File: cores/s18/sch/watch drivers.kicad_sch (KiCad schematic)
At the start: 10 parts, among them Q10 74LS367, T10 74LS163, T11 PAL16L8

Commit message: wip cer
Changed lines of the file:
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@@
     (stroke (width 0) (type default) (color 0 0 0 0))
   )
-  (wire (pts (xy 215.9 85.09) (xy 204.47 85.09))
+  (wire (pts (xy 207.01 85.09) (xy 204.47 85.09))
     (stroke (width 0) (type default) (color 0 0 0 0))
   )
@@
     (effects (font (size 1.27 1.27)) (justify left bottom))
   )
-  (label "~{RST_CLK}" (at 215.9 85.09 180)
-    (effects (font (size 1.27 1.27)) (justify right bottom))
-  )
   (label "VSS" (at 182.88 64.77 0)
     (effects (font (size 1.27 1.27)) (justify left bottom))
@@
     (effects (font (size 1.27 1.27)) (justify left))
   )
+  (hierarchical_label "~{RST_CLK}" (shape tri_state) (at 207.01 85.09 0)
+    (effects (font (size 1.27 1.27)) (justify left))
+  )

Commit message: finished extraction of s18
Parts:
- removed 4.7kΩ: R31, symbol Device:R_US
- added R31: 4.7KΩ, symbol Device:R_US
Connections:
- net VCC: now also R31.1
- net ~{CSYNC}: now also R31.2
- net COUN_~{MR} renamed SPRPAL8
- net COUN_~{MR}B renamed MAPP_WR_H
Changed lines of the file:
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@@
     (rev "José Tejada G.")
     (company "JOTEGO")
-    (comment 1 "Esperanza Triana")
+    (comment 1 "patreon.com/jotego")
+    (comment 2 "Esperanza Triana")
   )
   (junction (at 60.96 138.43) (diameter 0) (color 0 0 0 0)
   )
+  (junction (at 146.05 110.49) (diameter 0) (color 0 0 0 0)
+  )
   (junction (at 60.96 87.63) (diameter 0) (color 0 0 0 0)
   )
@@
   )
   (junction (at 60.96 125.73) (diameter 0) (color 0 0 0 0)
-  )
-  (junction (at 146.05 110.49) (diameter 0) (color 0 0 0 0)
   )
   (junction (at 60.96 88.9) (diameter 0) (color 0 0 0 0)
@@
   (no_connect (at 146.05 125.73))
   (no_connect (at 182.88 53.34))
+  (bus_entry (at 46.99 106.68) (size 2.54 2.54)
+    (stroke (width 0) (type default) (color 0 0 0 0))
+  )
   (wire (pts (xy 115.57 130.81) (xy 115.57 152.4))
     (stroke (width 0) (type default) (color 0 0 0 0))
@@
     (stroke (width 0) (type default) (color 0 0 0 0))
   )
-  (wire (pts (xy 185.42 80.01) (xy 172.72 80.01))
+  (wire (pts (xy 185.42 80.01) (xy 180.34 80.01))
     (stroke (width 0) (type default) (color 0 0 0 0))
   )
@@
     (stroke (width 0) (type default) (color 0 0 0 0))
   )
-  (wire (pts (xy 50.8 147.32) (xy 60.96 147.32))
+  (wire (pts (xy 41.91 147.32) (xy 60.96 147.32))
     (stroke (width 0) (type default) (color 0 0 0 0))
   )
@@
     (stroke (width 0) (type default) (color 0 0 0 0))
   )
+  (bus (pts (xy 41.91 106.68) (xy 46.99 106.68))
+    (stroke (width 0) (type default) (color 0 0 0 0))
+  )
   (wire (pts (xy 100.33 88.9) (xy 100.33 93.98))
     (stroke (width 0) (type default) (color 0 0 0 0))
@@
     (stroke (width 0) (type default) (color 0 0 0 0))
   )
-  (image (at 275.59 175.26) (scale 0.25)
+  (image (at 276.86 173.99) (scale 0.198066)
     (data
       iVBORw0KGgoAAAANSUhEUgAAAxoAAAMaCAIAAACOIqcFAAAAA3NCSVQICAjb4U/gAAAACXBIWXMA
@@
     (effects (font (size 1.27 1.27)) (justify right bottom))
   )
-  (label "COUN_~{MR}B" (at 110.49 128.27 0)
-    (effects (font (size 1.27 1.27)) (justify left bottom))
-  )
   (label "VSS" (at 162.56 52.07 180)
     (effects (font (size 1.27 1.27)) (justify right bottom))
   )
-  (label "COUN_~{MR}" (at 110.49 120.65 0)
-    (effects (font (size 1.27 1.27)) (justify left bottom))
-  )
-  (label "COUN_~{MR}B" (at 50.8 147.32 0)
+  (label "SPRPAL8" (at 110.49 120.65 0)
     (effects (font (size 1.27 1.27)) (justify left bottom))
   )
@@
     (effects (font (size 1.27 1.27)) (justify left bottom))
   )
-  (label "COUN_~{MR}" (at 110.49 83.82 0)
+  (label "SPRPAL8" (at 110.49 83.82 0)
+    (effects (font (size 1.27 1.27)) (justify left bottom))
+  )
+  (label "MAPP_WR_H" (at 110.49 128.27 0)
     (effects (font (size 1.27 1.27)) (justify left bottom))
   )
@@
     (effects (font (size 1.27 1.27)) (justify right bottom))
   )
+  (label "SPRPAL8" (at 49.53 109.22 0)
+    (effects (font (size 1.27 1.27)) (justify left bottom))
+  )
   (label "VCC" (at 53.34 100.33 0)
     (effects (font (size 1.27 1.27)) (justify left bottom))
@@
     (effects (font (size 1.27 1.27)) (justify left bottom))
   )
-  (label "~{RESET}" (at 172.72 80.01 0)
-    (effects (font (size 1.27 1.27)) (justify left bottom))
-  )
-  (label "COUN_~{MR}B" (at 110.49 128.27 0)
-    (effects (font (size 1.27 1.27)) (justify left bottom))
-  )
   (label "VSS" (at 180.34 100.33 0)
     (effects (font (size 1.27 1.27)) (justify left bottom))
@@
   )
   (label "VSS" (at 53.34 125.73 0)
-    (effects (font (size 1.27 1.27)) (justify left bottom))
-  )
-  (label "COUN_~{MR}" (at 49.53 109.22 0)
     (effects (font (size 1.27 1.27)) (justify left bottom))
   )
@@
     (effects (font (size 1.27 1.27)) (justify left))
   )
+  (hierarchical_label "SPRPAL[10..1]" (shape input) (at 41.91 106.68 180)
+    (effects (font (size 1.27 1.27)) (justify right))
+  )
   (hierarchical_label "~{VSYNC}" (shape input) (at 180.34 82.55 180)
     (effects (font (size 1.27 1.27)) (justify right))
@@
     (effects (font (size 1.27 1.27)) (justify right))
   )
+  (hierarchical_label "~{RESET}" (shape input) (at 180.34 80.01 180)
+    (effects (font (size 1.27 1.27)) (justify right))
+  )
   (hierarchical_label "SYNC" (shape tri_state) (at 213.36 43.18 0)
     (effects (font (size 1.27 1.27)) (justify left))
@@
   )
   (hierarchical_label "PRE_SYNC" (shape input) (at 176.53 43.18 180)
+    (effects (font (size 1.27 1.27)) (justify right))
+  )
+  (hierarchical_label "MAPP_WR_H" (shape input) (at 41.91 147.32 180)
     (effects (font (size 1.27 1.27)) (justify right))
   )
@@
     (pin "7")
   )
+  (symbol (lib_id "Device:R_US") (at 146.05 114.3 0) (unit 1)
+    (in_bom yes) (on_board yes)
+    (property "Reference" "R31" (id 0) (at 149.86 113.03 0))
+    (property "Value" "4.7KΩ" (id 1) (at 149.86 115.57 0))
+    (property "Footprint" "" (id 2) (at 147.066 114.554 90)
+      (effects (font (size 1.27 1.27)) hide)
+    )
+    (property "Datasheet" "~" (id 3) (at 146.05 114.3 0)
+      (effects (font (size 1.27 1.27)) hide)
+    )
+    (pin "1")
+    (pin "2")
+  )
   (symbol (lib_id "jt74:74LS163") (at 73.66 96.52 0) (unit 1)
     (in_bom yes) (on_board yes)
@@
     (pin "9")
   )
-  (symbol (lib_id "Device:R_US") (at 146.05 114.3 0) (unit 1)
-    (in_bom yes) (on_board yes)
-    (property "Reference" "4.7kΩ" (id 0) (at 149.86 116.84 0))
-    (property "Value" "R31" (id 1) (at 148.59 114.3 0))
-    (property "Footprint" "" (id 2) (at 147.066 114.554 90)
-      (effects (font (size 1.27 1.27)) hide)
-    )
-    (property "Datasheet" "~" (id 3) (at 146.05 114.3 0)
-      (effects (font (size 1.27 1.27)) hide)
-    )
-    (pin "1")
-    (pin "2")
-  )
   (symbol (lib_id "Device:C_Small") (at 162.56 45.72 0) (mirror y) (unit 1)

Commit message: s18: wip
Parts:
- N11: value XTAL48GHz -> XTAL48MHz
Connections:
- net SND_~{CLK} renamed CLK8
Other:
- note added: "16 MHz"

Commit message: s18 sch: more cleaning
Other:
- title: System 18  MODEL 837-7178 -> SEGA System 18  MODEL 837-7178
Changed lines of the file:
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@@
   (paper "A4")
   (title_block
-    (title "System 18  MODEL 837-7178")
+    (title "SEGA System 18  MODEL 837-7178")
     (date "2022-03-18")
     (rev "José Tejada G.")

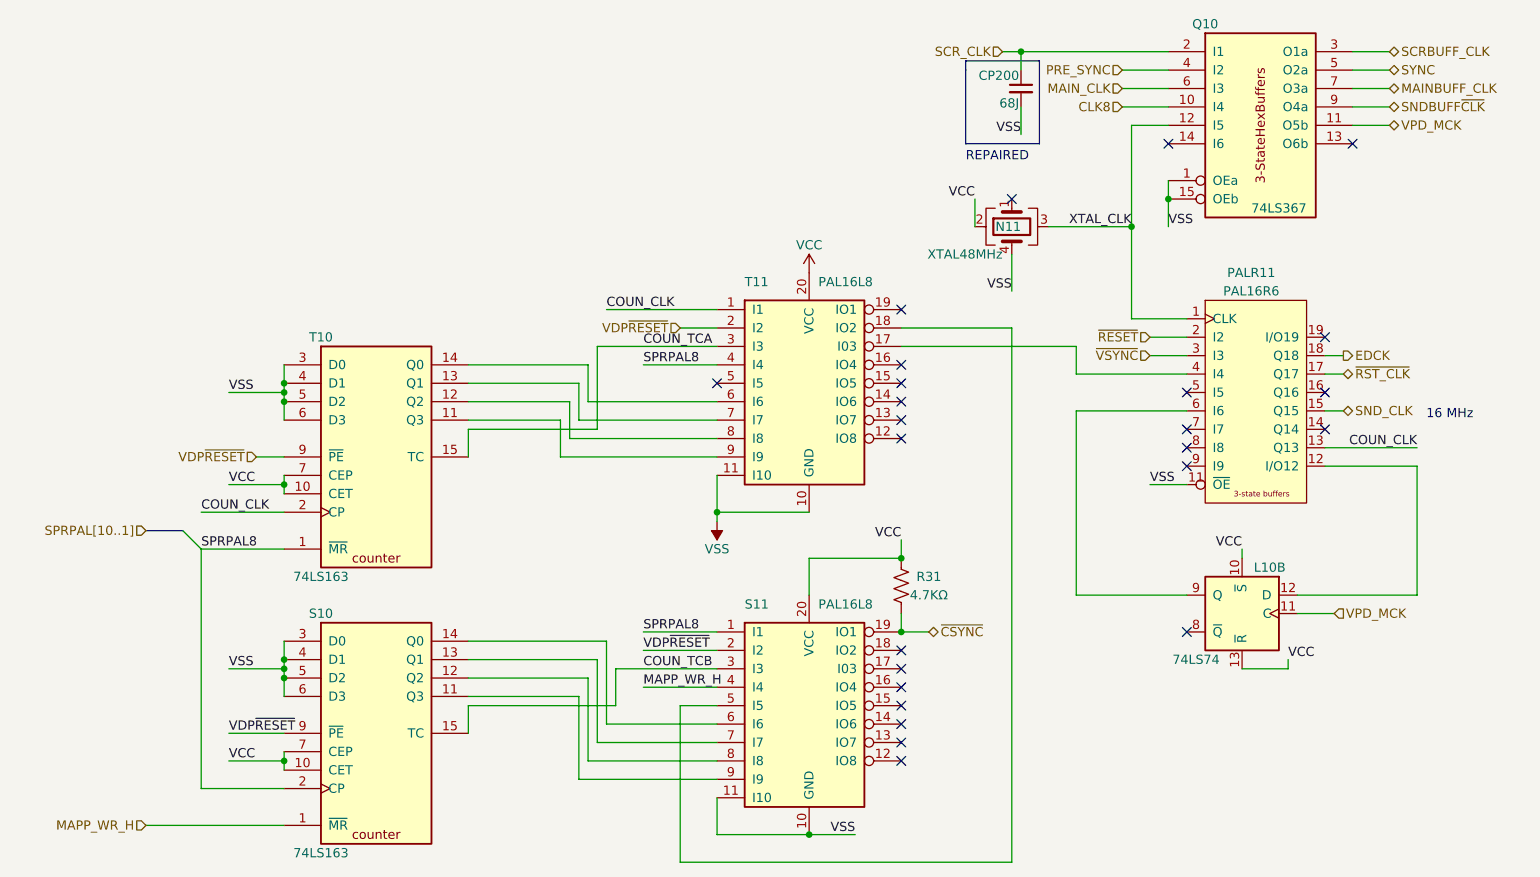
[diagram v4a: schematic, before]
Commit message: s18: added Nuked-MD's VDP module
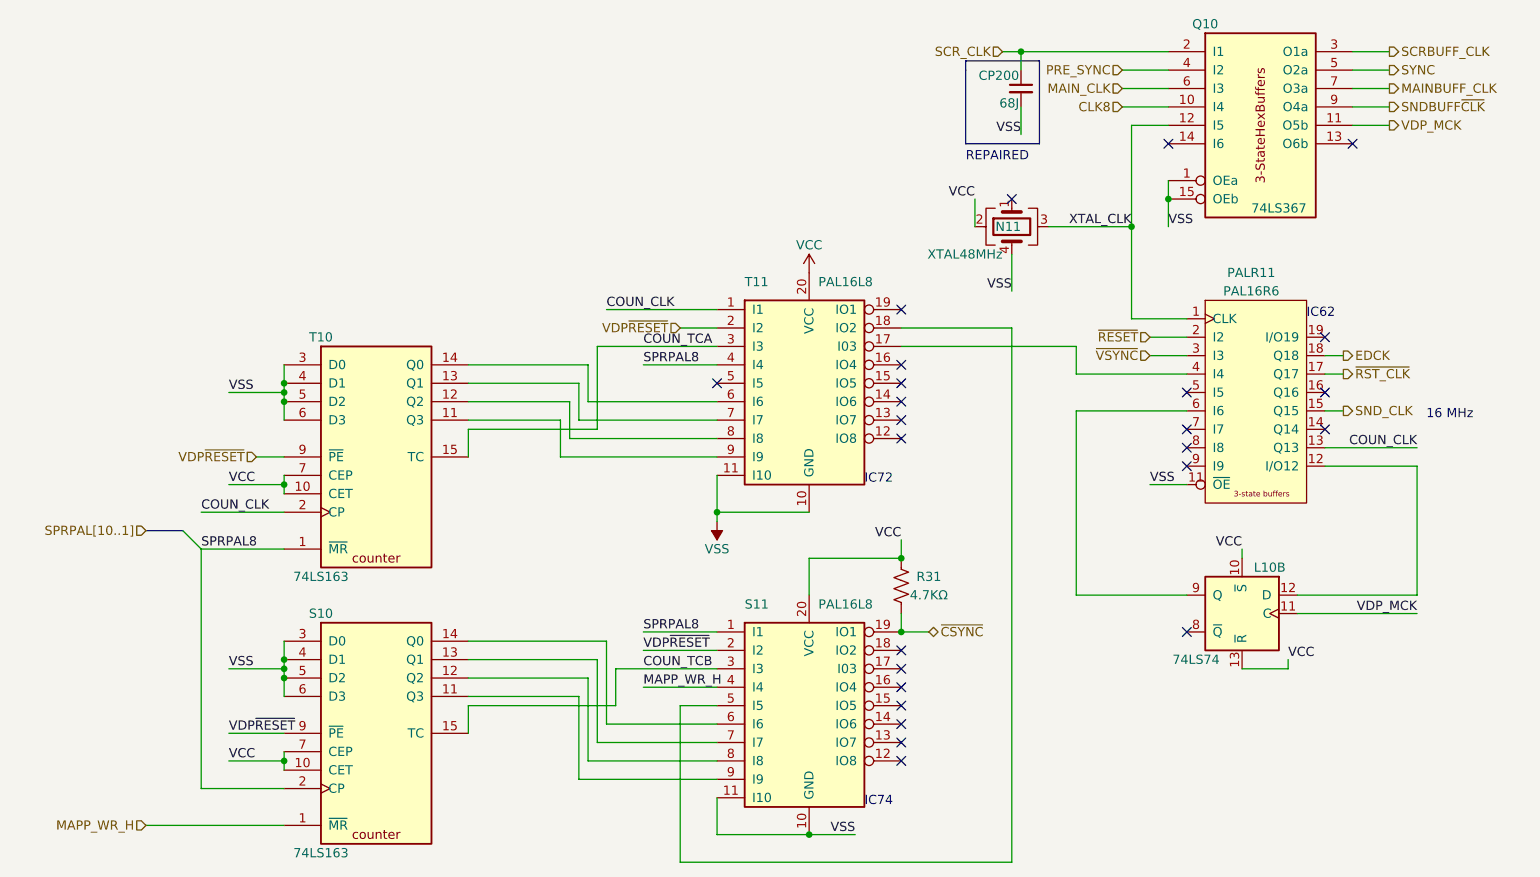
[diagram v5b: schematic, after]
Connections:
- net VPD_MCK renamed VDP_MCK
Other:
- note added: "IC62"
- note added: "IC72"
- note added: "IC74"
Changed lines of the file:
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@@
-    (stroke (width 0) (type default))
-  )
-  (wire (pts (xy 205.74 118.11) (xy 200.66 118.11))
     (stroke (width 0) (type default))
   )
@@
   )
   (wire (pts (xy 204.47 95.25) (xy 217.17 95.25))
+    (stroke (width 0) (type default))
+  )
+  (wire (pts (xy 200.66 118.11) (xy 217.17 118.11))
     (stroke (width 0) (type default))
   )
@@
     (effects (font (size 1.27 1.27)) (justify left bottom))
   )
+  (text "IC62" (at 201.93 77.47 0)
+    (effects (font (size 1.27 1.27)) (justify left bottom))
+  )
+  (text "IC74" (at 140.97 144.78 0)
+    (effects (font (size 1.27 1.27)) (justify left bottom))
+  )
+  (text "IC72" (at 140.97 100.33 0)
+    (effects (font (size 1.27 1.27)) (justify left bottom))
+  )
   (label "VCC" (at 193.04 109.22 180) (fields_autoplaced)
     (effects (font (size 1.27 1.27)) (justify right bottom))
@@
     (effects (font (size 1.27 1.27)) (justify right bottom))
   )
+  (label "VDP_MCK" (at 217.17 118.11 180) (fields_autoplaced)
+    (effects (font (size 1.27 1.27)) (justify right bottom))
+  )
   (label "COUN_TCA" (at 110.49 81.28 0) (fields_autoplaced)
     (effects (font (size 1.27 1.27)) (justify left bottom))
@@
     (effects (font (size 1.27 1.27)) (justify left bottom))
   )
-  (hierarchical_label "VPD_MCK" (shape input) (at 205.74 118.11 0) (fields_autoplaced)
+  (hierarchical_label "SPRPAL[10..1]" (shape input) (at 41.91 106.68 180) (fields_autoplaced)
+    (effects (font (size 1.27 1.27)) (justify right))
+  )
+  (hierarchical_label "~{VSYNC}" (shape input) (at 180.34 82.55 180) (fields_autoplaced)
+    (effects (font (size 1.27 1.27)) (justify right))
+  )
+  (hierarchical_label "SCRBUFF_CLK" (shape output) (at 213.36 40.64 0) (fields_autoplaced)
     (effects (font (size 1.27 1.27)) (justify left))
   )
-  (hierarchical_label "SPRPAL[10..1]" (shape input) (at 41.91 106.68 180) (fields_autoplaced)
-    (effects (font (size 1.27 1.27)) (justify right))
-  )
-  (hierarchical_label "~{VSYNC}" (shape input) (at 180.34 82.55 180) (fields_autoplaced)
-    (effects (font (size 1.27 1.27)) (justify right))
-  )
-  (hierarchical_label "SCRBUFF_CLK" (shape tri_state) (at 213.36 40.64 0) (fields_autoplaced)
+  (hierarchical_label "SND_CLK" (shape output) (at 207.01 90.17 0) (fields_autoplaced)
     (effects (font (size 1.27 1.27)) (justify left))
   )
-  (hierarchical_label "SND_CLK" (shape tri_state) (at 207.01 90.17 0) (fields_autoplaced)
-    (effects (font (size 1.27 1.27)) (justify left))
-  )
-  (hierarchical_label "VPD_MCK" (shape tri_state) (at 213.36 50.8 0) (fields_autoplaced)
+  (hierarchical_label "VDP_MCK" (shape output) (at 213.36 50.8 0) (fields_autoplaced)
     (effects (font (size 1.27 1.27)) (justify left))
   )
@@
     (effects (font (size 1.27 1.27)) (justify right))
   )
-  (hierarchical_label "SYNC" (shape tri_state) (at 213.36 43.18 0) (fields_autoplaced)
+  (hierarchical_label "SYNC" (shape output) (at 213.36 43.18 0) (fields_autoplaced)
     (effects (font (size 1.27 1.27)) (justify left))
   )
-  (hierarchical_label "~{RST_CLK}" (shape tri_state) (at 207.01 85.09 0) (fields_autoplaced)
+  (hierarchical_label "~{RST_CLK}" (shape output) (at 207.01 85.09 0) (fields_autoplaced)
     (effects (font (size 1.27 1.27)) (justify left))
   )
-  (hierarchical_label "MAINBUFF_CLK" (shape tri_state) (at 213.36 45.72 0) (fields_autoplaced)
+  (hierarchical_label "MAINBUFF_CLK" (shape output) (at 213.36 45.72 0) (fields_autoplaced)
     (effects (font (size 1.27 1.27)) (justify left))
   )
@@
     (effects (font (size 1.27 1.27)) (justify right))
   )
-  (hierarchical_label "SNDBUFF~{CLK}" (shape tri_state) (at 213.36 48.26 0) (fields_autoplaced)
+  (hierarchical_label "SNDBUFF~{CLK}" (shape output) (at 213.36 48.26 0) (fields_autoplaced)
     (effects (font (size 1.27 1.27)) (justify left))
   )
